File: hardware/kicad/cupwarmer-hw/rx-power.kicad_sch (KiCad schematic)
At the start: 41 parts, among them J1 I2C Service, J3 STATUS_MON, U1 STWLC38JRM

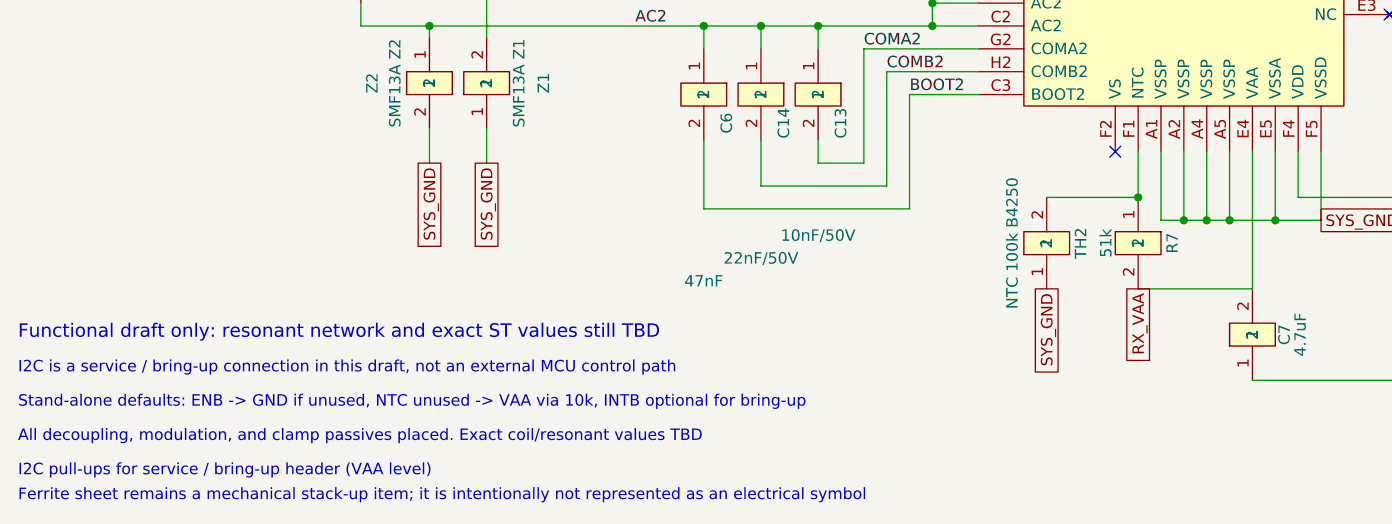
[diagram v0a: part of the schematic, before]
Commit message: Add heater harness NTC routing
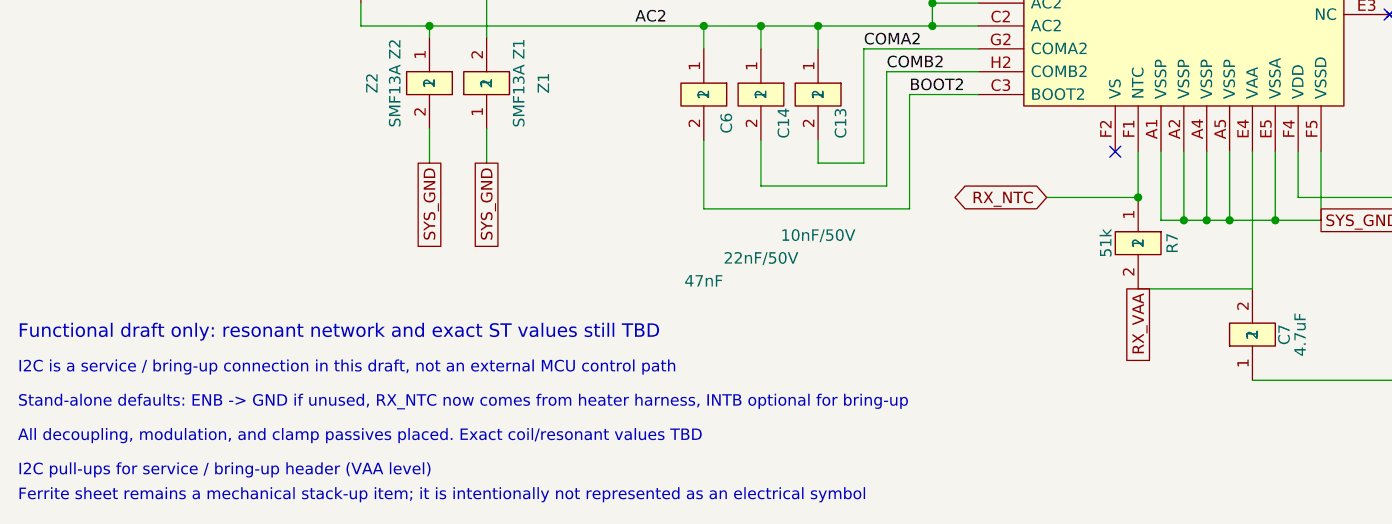
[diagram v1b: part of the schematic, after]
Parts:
- removed TH2: NTC 100k B4250, Resistor_SMD:R_0603_1608Metric, symbol cupwarmer:PASSIVE_2
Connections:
- net RX_NTC: now reaches R7.1, U1.F1 (NTC)
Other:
- note added: "Stand-alone defaults: ENB -> GND if unused, RX_NTC now comes from heater harness, INTB optional for bring-up"
- note removed: "Stand-alone defaults: ENB -> GND if unused, NTC unused -> VAA via 10k, INTB optional for bring-up"
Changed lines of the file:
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@@
 		)
 	)
-	(text "Stand-alone defaults: ENB -> GND if unused, NTC unused -> VAA via 10k, INTB optional for bring-up"
+	(text "Stand-alone defaults: ENB -> GND if unused, RX_NTC now comes from heater harness, INTB optional for bring-up"
 		(exclude_from_sim no)
 		(at 20.32 155.62 0)
@@
 		)
 	)
-	(global_label "SYS_GND"
-		(shape passive)
-		(at 134.62 142.24 270)
+	(global_label "RX_NTC"
+		(shape bidirectional)
+		(at 134.62 132.08 180)
 		(effects
 			(font
@@
 		)
 		(property "Intersheetrefs" "${INTERSHEET_REFS}"
-			(at 134.62 142.24 90)
+			(at 134.62 132.08 0)
 			(hide yes)
 			(show_name no)
@@
 			)
 		)
-		(property "Description" "NTC pull-up to VAA (51k); forms divider with 100k TH2 for STWLC38 OTP (~69C typ, VNTC,OTP=0.59V)"
+		(property "Description" "NTC pull-up to RX_VAA (51k); forms divider with external 100k/B4260 heater NTC on RX_NTC for STWLC38 OTP (~69C typ, VNTC,OTP=0.59V)"
 			(at 144.78 137.16 180)
 			(hide yes)
@@
 					(unit 1)
 				)
-			)
-		)
-	)
-	(symbol
-		(lib_id "cupwarmer:PASSIVE_2")
-		(at 134.62 137.16 90)
-		(unit 1)
-		(body_style 1)
-		(exclude_from_sim no)
-		(in_bom yes)
-		(on_board yes)
-		(in_pos_files yes)
-		(dnp no)
-		(property "Reference" "TH2"
-			(at 138.43 137.16 0)
-			(show_name no)
-			(do_not_autoplace no)
-			(effects
-				(font
-					(size 1.27 1.27)
-				)
-			)
-		)
-		(property "Value" "NTC 100k B4250"
-			(at 130.81 137.16 0)
-			(show_name no)
-			(do_not_autoplace no)
-			(effects
-				(font
-					(size 1.27 1.27)
-				)
-			)
-		)
-		(property "Footprint" "Resistor_SMD:R_0603_1608Metric"
-			(at 134.62 137.16 0)
-			(hide yes)
-			(show_name no)
-			(do_not_autoplace no)
-			(effects
-				(font
-					(size 1.27 1.27)
-				)
-			)
-		)
-		(property "Datasheet" "~"
-			(at 134.62 137.16 0)
-			(hide yes)
-			(show_name no)
-			(do_not_autoplace no)
-			(effects
-				(font
-					(size 1.27 1.27)
-				)
-			)
-		)
-		(property "Description" "RX_NTC for STWLC38 internal OTP; matches ST eval reference"
-			(at 134.62 137.16 0)
-			(hide yes)
-			(show_name no)
-			(do_not_autoplace no)
-			(effects
-				(font
-					(size 1.27 1.27)
-				)
-			)
-		)
-		(property "Manufacturer" "Murata Electronics"
-			(at -40.64 213.36 0)
-			(hide yes)
-			(show_name no)
-			(do_not_autoplace no)
-			(effects
-				(font
-					(size 1.27 1.27)
-				)
-			)
-		)
-		(property "LCSC" "C71280"
-			(at -40.64 213.36 0)
-			(hide yes)
-			(show_name no)
-			(do_not_autoplace no)
-			(effects
-				(font
-					(size 1.27 1.27)
-				)
-			)
-		)
-		(property "MPN" "NCP18WF104F12RB"
-			(at -40.64 213.36 0)
-			(hide yes)
-			(show_name no)
-			(do_not_autoplace no)
-			(effects
-				(font
-					(size 1.27 1.27)
-				)
-			)
-		)
-		(pin "1"
-		)
-		(pin "2"
-		)
-		(instances
-			(project "rx-power"
-				(path "/11111111-aaaa-bbbb-cccc-111111111111"
-					(reference "TH2")
-					(unit 1)
-				)
-			)
-			(project "cupwarmer-hw"
-				(path "/f3c63676-f392-4700-9f58-a6787e1eb284/11111111-1111-1111-1111-111111111111"
-					(reference "TH2")
-					(unit 1)
-				)
